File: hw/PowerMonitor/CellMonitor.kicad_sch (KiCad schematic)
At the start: 25 parts, among them Q1 Q_PMOS_GDS, U5 LM358, U6 LM358, U7 LM358, U8 LM393, U9 74LVC1G32

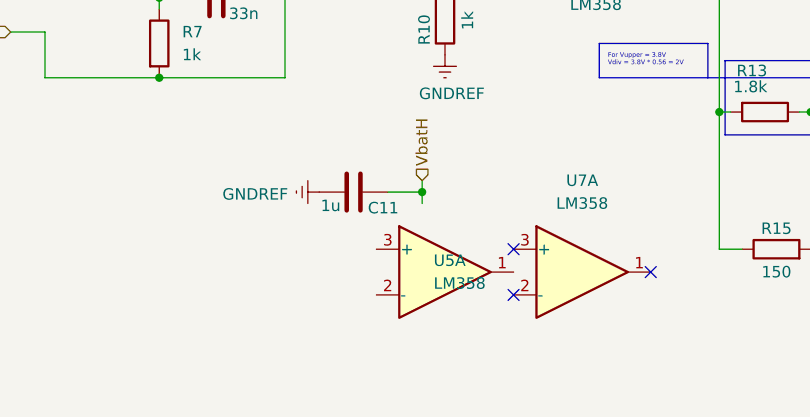
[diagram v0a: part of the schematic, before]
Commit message: finish fmu routing
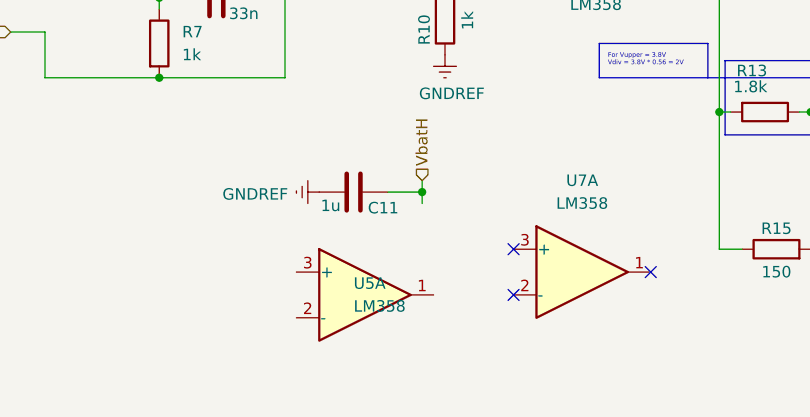
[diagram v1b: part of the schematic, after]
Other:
- moved on the sheet: U5A
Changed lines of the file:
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@@
 	(symbol
 		(lib_id "Amplifier_Operational:LM358")
-		(at 107.95 119.38 0)
+		(at 99.06 121.92 0)
 		(unit 1)
 		(exclude_from_sim no)
@@
 		(fields_autoplaced yes)
 		(property "Reference" "U5"
-			(at 106.68 118.1099 0)
+			(at 97.79 120.6499 0)
 			(effects
 				(font
@@
 		)
 		(property "Value" "LM358"
-			(at 106.68 120.6499 0)
+			(at 97.79 123.1899 0)
 			(effects
 				(font
@@
 		)
 		(property "Footprint" "Package_SO:SOIC-8_3.9x4.9mm_P1.27mm"
-			(at 107.95 119.38 0)
+			(at 99.06 121.92 0)
 			(effects
 				(font
@@
 		)
 		(property "Datasheet" "http://www.ti.com/lit/ds/symlink/lm2904-n.pdf"
-			(at 107.95 119.38 0)
+			(at 99.06 121.92 0)
 			(effects
 				(font
@@
 		)
 		(property "Description" "Low-Power, Dual Operational Amplifiers, DIP-8/SOIC-8/TO-99-8"
-			(at 107.95 119.38 0)
+			(at 99.06 121.92 0)
 			(effects
 				(font
@@
 		)
 		(property "PN" "LM358-TD"
-			(at 107.95 119.38 0)
+			(at 99.06 121.92 0)
 			(effects
 				(font
